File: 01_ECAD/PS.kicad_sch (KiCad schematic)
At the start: 76 parts, among them J1 B2P3-VH(LF)(SN), J2 B4P-VH(LF)(SN), Q1 IXFH20N100P, SW1 NE18 2A EE 6AMP, U1 UCC28600, U2 CNY17-1, U3 TL431DBZ

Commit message: Changing Mosfet.
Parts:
- added D2: PMEG100T10ELXDX, Diode_SMD:D_SOD-323, symbol Diode:UF5407
- added R2: 4.7, Resistor_SMD:R_0603_1608Metric, symbol Device:R_Small_US
- Q1: value IXFH20N100P -> IXFH20N100PSIHA6N80AE-GE3; footprint Package_TO_SOT_THT:TO-247-3_Vertical -> PS:TO-220-3_Vertical
- renumbered C27 to C12, C12 to C13, C13 to C14, C14 to C15, C15 to C16, C16 to C17, C17 to C18, C18 to C19, C19 to C20, C20 to C21, C21 to C22, C22 to C23, C23 to C24, C24 to C25, C25 to C26, C26 to C27, D2 to D3, D3 to D4, D4 to D5, D5 to D6, D6 to D7, D7 to D8, R2 to R1, R9 to R10, R10 to R11, R11 to R12, R12 to R13, R13 to R14, R14 to R15, R15 to R16, R19 to R17, R16 to R18, R17 to R19, R18 to R20, R20 to R21, R1 to R3, R3 to R4, R4 to R5, R5 to R6, R6 to R7, R7 to R8, R8 to R9
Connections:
- net TR_GAT: now also D2.2 (A); no longer R3.2
- net at Q1.1 (G), R3.1, R4.1: now also R2.1; no longer D1.2 (A)
- net at C3.1, C4.1, C5.1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: now also D3.1 (K); no longer R9.2
- net at R9.1: now also C6.1, D4.1 (K); no longer D3.1 (K)
- new net: D2.1 (K), R3.2
- new net: D3.2 (A), R9.2
- new net: D1.2 (A), R2.2
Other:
- moved on the sheet: D1, D3, R1, R3, R9

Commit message: Update.
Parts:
- HS1: value WV-T247-101E -> 504222B00000G; footprint PS:WV-T247-101E -> (none)
- Q1: value IXFH20N100PSIHA6N80AE-GE3 -> SIHA6N80AE-GE3; footprint PS:TO-220-3_Vertical -> PS:SIHA6N80AE-GE3
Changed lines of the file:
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@@
 			)
 		)
-		(property "Value" "IXFH20N100PSIHA6N80AE-GE3"
+		(property "Value" "SIHA6N80AE-GE3"
 			(at 81.915 170.815 90)
 			(effects
@@
 			)
 		)
-		(property "Footprint" "PS:TO-220-3_Vertical"
+		(property "Footprint" "PS:SIHA6N80AE-GE3"
 			(at 81.28 162.56 0)
 			(effects
@@
 		(exclude_from_sim no)
 		(in_bom yes)
-		(on_board yes)
+		(on_board no)
 		(dnp no)
 		(property "Reference" "HS1"
@@
 			)
 		)
-		(property "Value" "WV-T247-101E"
+		(property "Value" "504222B00000G"
 			(at 90.805 169.545 90)
 			(effects
@@
 			)
 		)
-		(property "Footprint" "PS:WV-T247-101E"
+		(property "Footprint" ""
 			(at 83.82 165.4048 0)
 			(effects
@@
 			)
 		)
-		(property "Datasheet" "529701B02100G"
+		(property "Datasheet" "504222B00000G"
 			(at 83.82 165.4048 0)
 			(effects
@@
 			(at 83.82 165.1 0)
 			(effects
+				(font
+					(size 1.27 1.27)
+				)
+				(hide yes)
+			)
+		)
+		(property "PN" ""
+			(at 83.82 165.1 0)
+			(effects

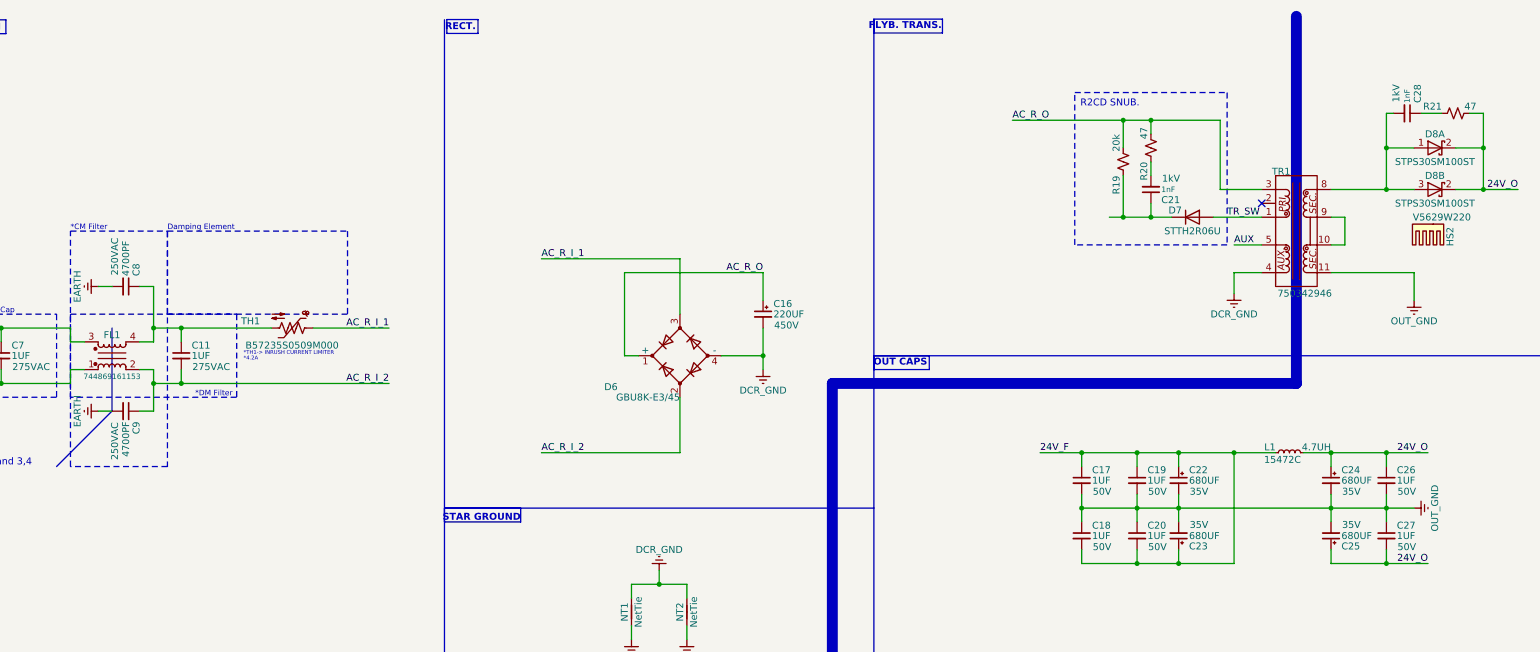
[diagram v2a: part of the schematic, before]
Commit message: Update from 150W to 120W.
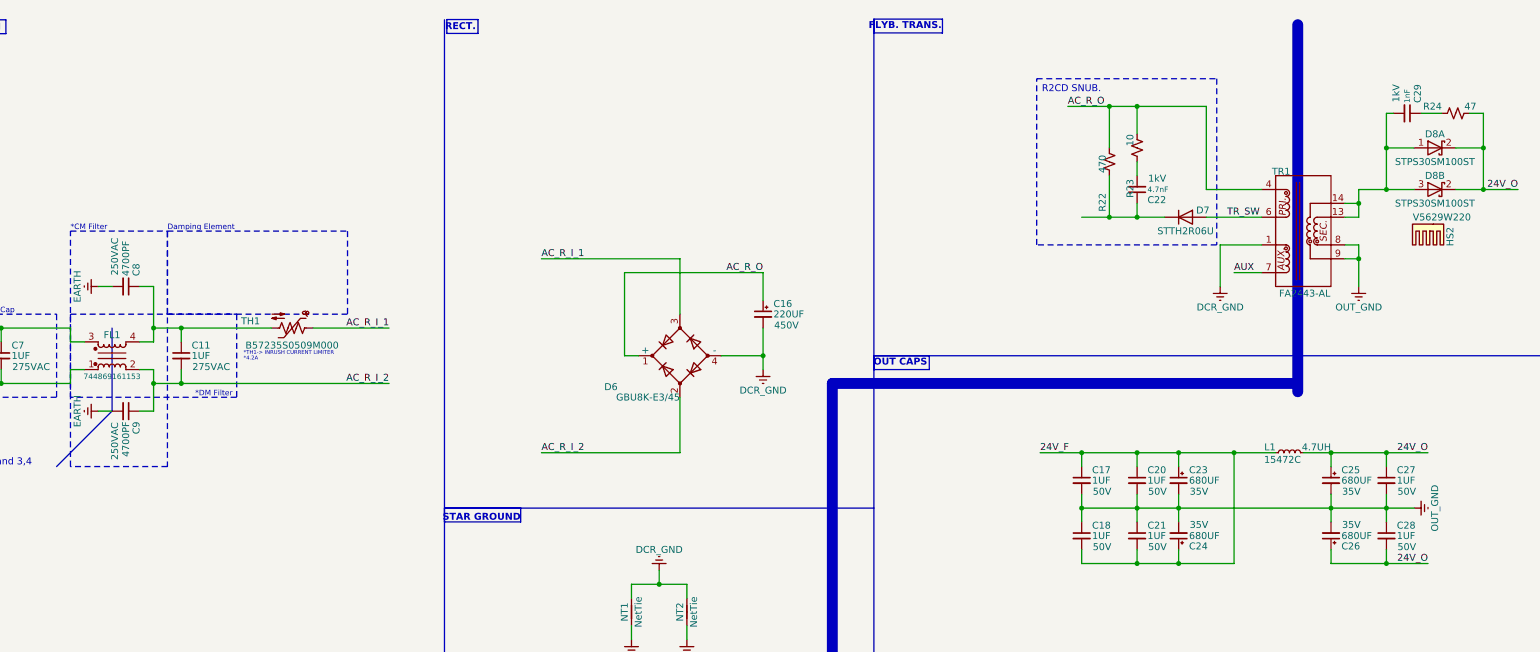
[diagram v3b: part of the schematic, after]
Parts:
- removed C21: 1nF, Capacitor_THT:C_Disc_D7.5mm_W5.0mm_P7.50mm, symbol ps:C_Small
- removed R20: 47, Resistor_THT:R_Axial_DIN0516_L15.5mm_D5.0mm_P5.08mm_Vertical, symbol Device:R_Small_US
- removed TR1: 750342946, PS:750342946, symbol ps:750342946
- added C22: 4.7nF, Capacitor_THT:C_Disc_D7.5mm_W5.0mm_P7.50mm, symbol ps:C_Small
- added R23: 10, Resistor_THT:R_Axial_DIN0516_L15.5mm_D5.0mm_P5.08mm_Vertical, symbol Device:R_Small_US
- added TR1: FA2443-AL, PS:FA2443-AL, symbol ps:FA2443-AL
- R22: renamed from R19; value 20k -> 470; PN (none) -> 13FR010E
- renumbered C19 to C20, C20 to C21, C22 to C23, C23 to C24, C24 to C25, C25 to C26, C26 to C27, C27 to C28, C28 to C29, R21 to R24
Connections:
- net AC_R_O: now also R23.2, TR1.4
- net AUX: now also TR1.7
- net DCR_GND: now also TR1.1
- net OUT_GND: now also TR1.8, TR1.9
- net TR_SW: now also TR1.6
- net at C29.2, D8.1 (A), D8.3 (K): now also TR1.13, TR1.14
- net at D7.1 (K), R22.1: now also C22.1
- new net: C22.2, R23.1
- no-connect marks 8 -> 7
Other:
- moved on the sheet: D7, R22

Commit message: Update.
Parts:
- R10: value 86.6k -> 200k; PN (none) -> ERA-3AEB204V
- R11: value 31.875k -> 39k; PN (none) -> ERA-3ARW393V
- TR1: PN (none) -> FA2443-AL
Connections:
- net DCR_GND: now also C12.2
- net GND_DC_P: no longer C12.2
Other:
- moved on the sheet: HS1, HS2

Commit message: Update.
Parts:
- C1, C2: VOLTAGE V -> 35V
- C3, C4, C5: PN (none) -> 0603W106M250XD; VOLTAGE V -> 25V
- C6: PN (none) -> EEU-FC1V680
- Q1: value SIHA6N80AE-GE3 -> SPP11N80C3XKSA1; footprint PS:SIHA6N80AE-GE3 -> SPP11N80C3XKSA1; PN (none) -> SPP11N80C3XKSA1
- R1: PN (none) -> RC0603FR-071K33L
- R10: PN ERA-3AEB204V -> RC0603JR-07200KL
- R11: PN ERA-3ARW393V -> RC0603JR-0739KL
- R2, R3: PN (none) -> RC1206JR-074R7L
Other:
- moved on the sheet: C1, C2
